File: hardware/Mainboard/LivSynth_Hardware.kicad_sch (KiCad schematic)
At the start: 0 parts

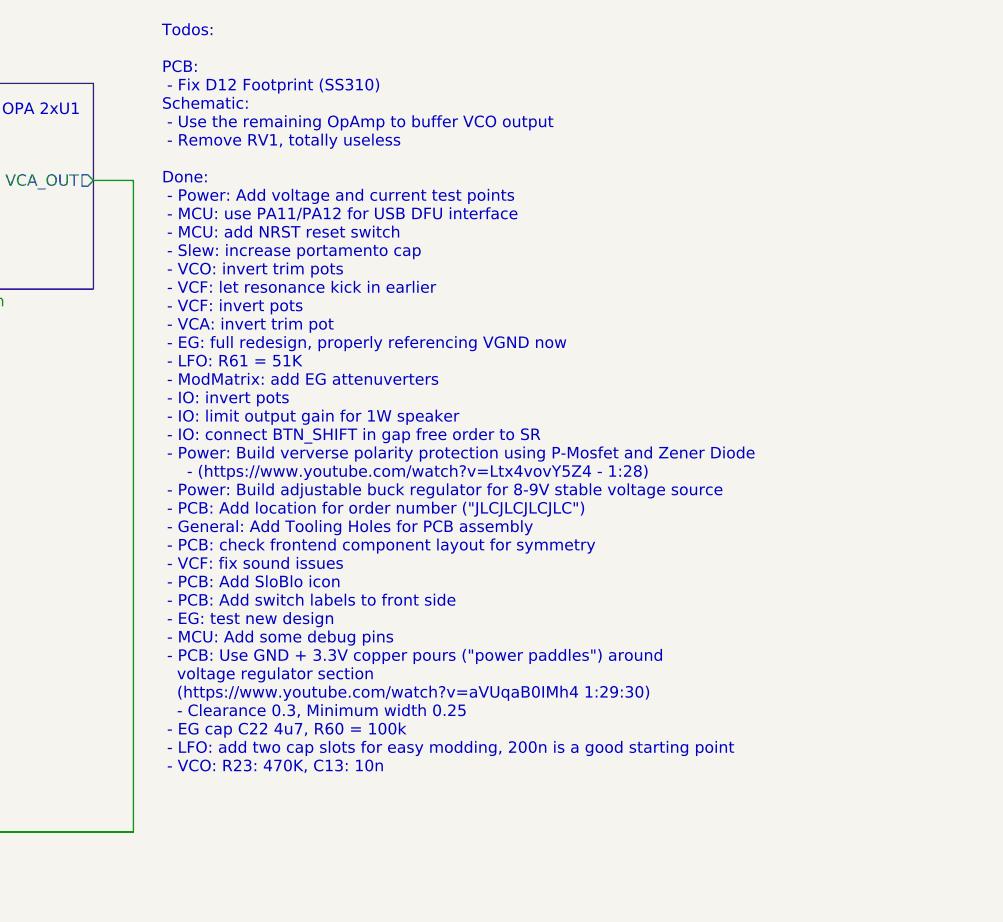
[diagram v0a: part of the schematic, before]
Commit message: add 0v2 status
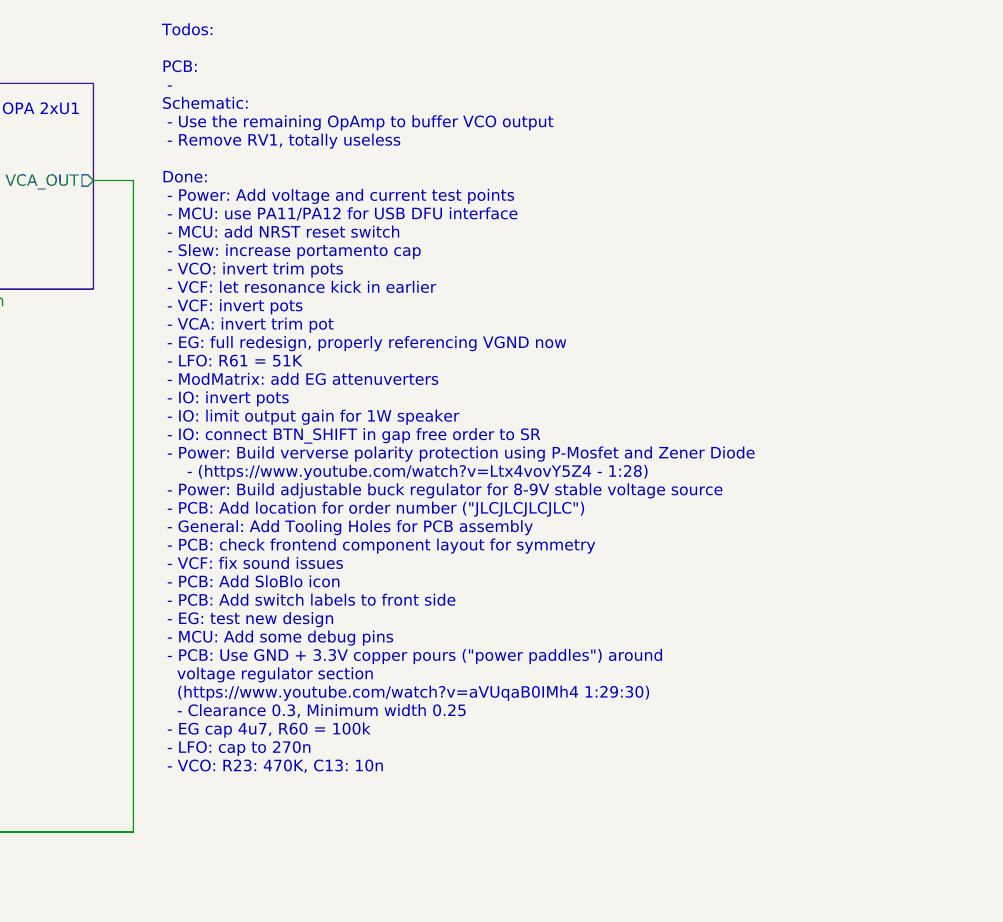
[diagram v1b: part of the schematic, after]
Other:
- note added: "Todos: PCB: - Schematic: - Use the remaining OpAmp to buffer VCO output - Remove RV1, totally useless Done: - Power: Add voltage and current test points - MCU: use PA11/PA12 for USB DFU interface - MCU: add NRST reset switch - Slew: increase portamento cap - VCO: invert trim pots - VCF: let resonance kick in earlier - VCF: invert pots - VCA: invert trim pot - EG: full redesign, properly referenci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"
- note removed: "Todos: PCB: - Fix D12 Footprint (SS310) Schematic: - Use the remaining OpAmp to buffer VCO output - Remove RV1, totally useless Done: - Power: Add voltage and current test points - MCU: use PA11/PA12 for USB DFU interface - MCU: add NRST reset switch - Slew: increase portamento cap - VCO: invert trim pots - VCF: let resonance kick in earlier - VCF: invert pots - VCA: invert trim pot - EG: full re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"
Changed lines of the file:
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@@
     (effects (font (size 1.27 1.27)) (justify left bottom))
   )
-  (text "Todos:\n\nPCB:\n - Fix D12 Footprint (SS310)\nSchematic:\n - Use the remaining OpAmp to buffer VCO output\n - Remove RV1, totally useless\n\nDone:\n - Power: Add voltage and current test points\n - MCU: use PA11/PA12 for USB DFU interface\n - MCU: add NRST reset switch\n - Slew: increase portamento cap\n - VCO: invert trim pots\n - VCF: let resonance kick in earlier\n - VCF: invert pots\n - VCA: invert trim pot\n - EG: full redesign, properly referencing VGND now\n - LFO: R61 = 51K\n - ModMatrix: add EG attenuverters\n - IO: invert pots\n - IO: limit output gain for 1W speaker\n - IO: connect BTN_SHIFT in gap free order to SR\n - Power: Build ververse polarity protection using P-Mosfet and Zener Diode\n     - (https://www.youtube.com/watch?v=Ltx4vovY5Z4 - 1:28)\n - Power: Build adjustable buck regulator for 8-9V stable voltage source\n - PCB: Add location for order number (\"JLCJLCJLCJLC\")\n - General: Add Tooling Holes for PCB assembly\n - PCB: check frontend component layout for symmetry\n - VCF: fix sound issues\n - PCB: Add SloBlo icon\n - PCB: Add switch labels to front side\n - EG: test new design\n - MCU: Add some debug pins\n - PCB: Use GND + 3.3V copper pours (\"power paddles\") around\n   voltage regulator section\n   (https://www.youtube.com/watch?v=aVUqaB0IMh4 1:29:30)\n   - Clearance 0.3, Minimum width 0.25\n - EG cap C22 4u7, R60 = 100k\n - LFO: add two cap slots for easy modding, 200n is a good starting point\n - VCO: R23: 470K, C13: 10n"
+  (text "Todos:\n\nPCB:\n - \nSchematic:\n - Use the remaining OpAmp to buffer VCO output\n - Remove RV1, totally useless\n\nDone:\n - Power: Add voltage and current test points\n - MCU: use PA11/PA12 for USB DFU interface\n - MCU: add NRST reset switch\n - Slew: increase portamento cap\n - VCO: invert trim pots\n - VCF: let resonance kick in earlier\n - VCF: invert pots\n - VCA: invert trim pot\n - EG: full redesign, properly referencing VGND now\n - LFO: R61 = 51K\n - ModMatrix: add EG attenuverters\n - IO: invert pots\n - IO: limit output gain for 1W speaker\n - IO: connect BTN_SHIFT in gap free order to SR\n - Power: Build ververse polarity protection using P-Mosfet and Zener Diode\n     - (https://www.youtube.com/watch?v=Ltx4vovY5Z4 - 1:28)\n - Power: Build adjustable buck regulator for 8-9V stable voltage source\n - PCB: Add location for order number (\"JLCJLCJLCJLC\")\n - General: Add Tooling Holes for PCB assembly\n - PCB: check frontend component layout for symmetry\n - VCF: fix sound issues\n - PCB: Add SloBlo icon\n - PCB: Add switch labels to front side\n - EG: test new design\n - MCU: Add some debug pins\n - PCB: Use GND + 3.3V copper pours (\"power paddles\") around\n   voltage regulator section\n   (https://www.youtube.com/watch?v=aVUqaB0IMh4 1:29:30)\n   - Clearance 0.3, Minimum width 0.25\n - EG cap 4u7, R60 = 100k\n - LFO: cap to 270n\n - VCO: R23: 470K, C13: 10n"
     (at 212.09 99.695 0)
     (effects (font (size 1.27 1.27)) (justify left bottom))

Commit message: Backport from 0v3
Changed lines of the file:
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@@
     (effects (font (size 1.27 1.27)) (justify left bottom))
   )
-  (text "Todos:\n\nPCB:\n - \nSchematic:\n - Use the remaining OpAmp to buffer VCO output\n - Remove RV1, totally useless\n\nDone:\n - Power: Add voltage and current test points\n - MCU: use PA11/PA12 for USB DFU interface\n - MCU: add NRST reset switch\n - Slew: increase portamento cap\n - VCO: invert trim pots\n - VCF: let resonance kick in earlier\n - VCF: invert pots\n - VCA: invert trim pot\n - EG: full redesign, properly referencing VGND now\n - LFO: R61 = 51K\n - ModMatrix: add EG attenuverters\n - IO: invert pots\n - IO: limit output gain for 1W speaker\n - IO: connect BTN_SHIFT in gap free order to SR\n - Power: Build ververse polarity protection using P-Mosfet and Zener Diode\n     - (https://www.youtube.com/watch?v=Ltx4vovY5Z4 - 1:28)\n - Power: Build adjustable buck regulator for 8-9V stable voltage source\n - PCB: Add location for order number (\"JLCJLCJLCJLC\")\n - General: Add Tooling Holes for PCB assembly\n - PCB: check frontend component layout for symmetry\n - VCF: fix sound issues\n - PCB: Add SloBlo icon\n - PCB: Add switch labels to front side\n - EG: test new design\n - MCU: Add some debug pins\n - PCB: Use GND + 3.3V copper pours (\"power paddles\") around\n   voltage regulator section\n   (https://www.youtube.com/watch?v=aVUqaB0IMh4 1:29:30)\n   - Clearance 0.3, Minimum width 0.25\n - EG cap 4u7, R60 = 100k\n - LFO: cap to 270n\n - VCO: R23: 470K, C13: 10n"
+  (text "Todos:\n\nPCB:\n - \nSchematic:\n - Use the remaining OpAmp to buffer VCO output\n - Remove RV1, totally useless\n\nDone:\n - Power: Add voltage and current test points\n - MCU: use PA11/PA12 for USB DFU interface\n - MCU: add NRST reset switch\n - Slew: increase portamento cap\n - VCO: invert trim pots\n - VCF: let resonance kick in earlier\n - VCF: invert pots\n - VCA: invert trim pot\n - EG: full redesign, properly referencing VGND now\n - LFO: R61 = 51K\n - ModMatrix: add EG attenuverters\n - IO: invert pots\n - IO: limit output gain for 1W speaker\n - IO: connect BTN_SHIFT in gap free order to SR\n - Power: Build ververse polarity protection using P-Mosfet and Zener Diode\n     - (https://www.youtube.com/watch?v=Ltx4vovY5Z4 - 1:28)\n - Power: Build adjustable buck regulator for 8-9V stable voltage source\n - PCB: Add location for order number (\"JLCJLCJLCJLC\")\n - General: Add Tooling Holes for PCB assembly\n - PCB: check frontend component layout for symmetry\n - VCF: fix sound issues\n - PCB: Add SloBlo icon\n - PCB: Add switch labels to front side\n - EG: test new design\n - MCU: Add some debug pins\n - PCB: Use GND + 3.3V copper pours (\"power paddles\") around\n   voltage regulator section\n   (https://www.youtube.com/watch?v=aVUqaB0IMh4 1:29:30)\n   - Clearance 0.3, Minimum width 0.25\n - EG cap C22 4u7, R60 = 100K\n - LFO: cap to 270n\n - VCO: R23: 470K, C13: 10n"
     (at 212.09 99.695 0)
     (effects (font (size 1.27 1.27)) (justify left bottom))

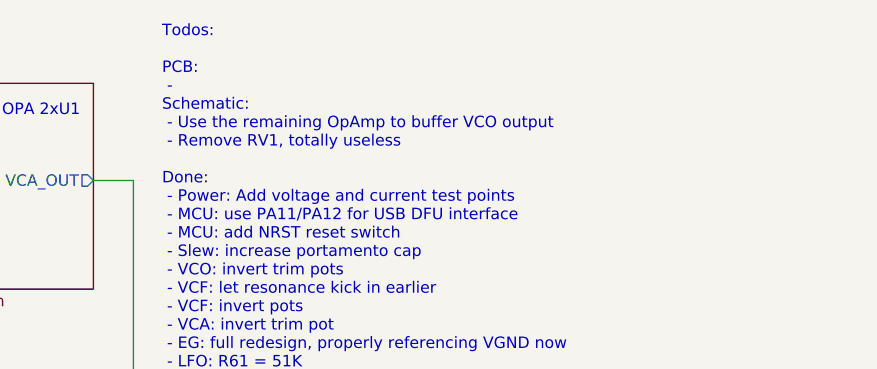
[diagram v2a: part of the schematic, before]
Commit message: Rename Decay -> Release
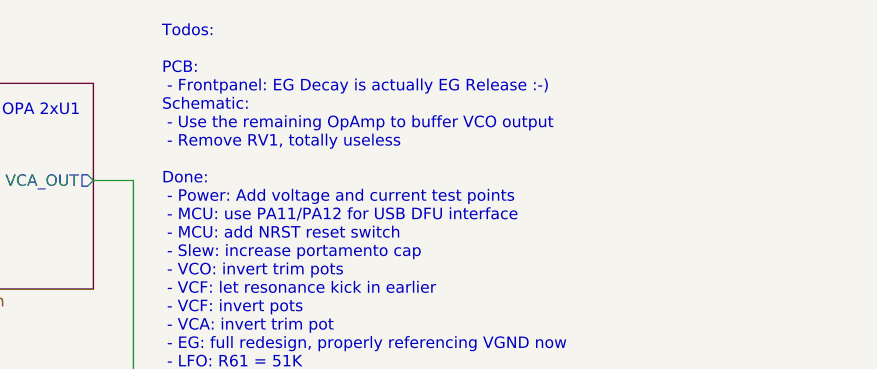
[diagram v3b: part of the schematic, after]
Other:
- note added: "Todos: PCB: - Frontpanel: EG Decay is actually EG Release :-) Schematic: - Use the remaining OpAmp to buffer VCO output - Remove RV1, totally useless Done: - Power: Add voltage and current test points - MCU: use PA11/PA12 for USB DFU interface - MCU: add NRST reset switch - Slew: increase portamento cap - VCO: invert trim pots - VCF: let resonance kick in earlier - VCF: invert pots - VCA: invert 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"
- note removed: "Todos: PCB: - Schematic: - Use the remaining OpAmp to buffer VCO output - Remove RV1, totally useless Done: - Power: Add voltage and current test points - MCU: use PA11/PA12 for USB DFU interface - MCU: add NRST reset switch - Slew: increase portamento cap - VCO: invert trim pots - VCF: let resonance kick in earlier - VCF: invert pots - VCA: invert trim pot - EG: full redesign, properly referenci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"
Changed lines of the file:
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@@
     (effects (font (size 1.27 1.27)) (justify left bottom))
   )
-  (text "Todos:\n\nPCB:\n - \nSchematic:\n - Use the remaining OpAmp to buffer VCO output\n - Remove RV1, totally useless\n\nDone:\n - Power: Add voltage and current test points\n - MCU: use PA11/PA12 for USB DFU interface\n - MCU: add NRST reset switch\n - Slew: increase portamento cap\n - VCO: invert trim pots\n - VCF: let resonance kick in earlier\n - VCF: invert pots\n - VCA: invert trim pot\n - EG: full redesign, properly referencing VGND now\n - LFO: R61 = 51K\n - ModMatrix: add EG attenuverters\n - IO: invert pots\n - IO: limit output gain for 1W speaker\n - IO: connect BTN_SHIFT in gap free order to SR\n - Power: Build ververse polarity protection using P-Mosfet and Zener Diode\n     - (https://www.youtube.com/watch?v=Ltx4vovY5Z4 - 1:28)\n - Power: Build adjustable buck regulator for 8-9V stable voltage source\n - PCB: Add location for order number (\"JLCJLCJLCJLC\")\n - General: Add Tooling Holes for PCB assembly\n - PCB: check frontend component layout for symmetry\n - VCF: fix sound issues\n - PCB: Add SloBlo icon\n - PCB: Add switch labels to front side\n - EG: test new design\n - MCU: Add some debug pins\n - PCB: Use GND + 3.3V copper pours (\"power paddles\") around\n   voltage regulator section\n   (https://www.youtube.com/watch?v=aVUqaB0IMh4 1:29:30)\n   - Clearance 0.3, Minimum width 0.25\n - EG cap C22 4u7, R60 = 100K\n - LFO: cap to 270n\n - VCO: R23: 470K, C13: 10n"
+  (text "Todos:\n\nPCB:\n - Frontpanel: EG Decay is actually EG Release :-)\nSchematic:\n - Use the remaining OpAmp to buffer VCO output\n - Remove RV1, totally useless\n\nDone:\n - Power: Add voltage and current test points\n - MCU: use PA11/PA12 for USB DFU interface\n - MCU: add NRST reset switch\n - Slew: increase portamento cap\n - VCO: invert trim pots\n - VCF: let resonance kick in earlier\n - VCF: invert pots\n - VCA: invert trim pot\n - EG: full redesign, properly referencing VGND now\n - LFO: R61 = 51K\n - ModMatrix: add EG attenuverters\n - IO: invert pots\n - IO: limit output gain for 1W speaker\n - IO: connect BTN_SHIFT in gap free order to SR\n - Power: Build ververse polarity protection using P-Mosfet and Zener Diode\n     - (https://www.youtube.com/watch?v=Ltx4vovY5Z4 - 1:28)\n - Power: Build adjustable buck regulator for 8-9V stable voltage source\n - PCB: Add location for order number (\"JLCJLCJLCJLC\")\n - General: Add Tooling Holes for PCB assembly\n - PCB: check frontend component layout for symmetry\n - VCF: fix sound issues\n - PCB: Add SloBlo icon\n - PCB: Add switch labels to front side\n - EG: test new design\n - MCU: Add some debug pins\n - PCB: Use GND + 3.3V copper pours (\"power paddles\") around\n   voltage regulator section\n   (https://www.youtube.com/watch?v=aVUqaB0IMh4 1:29:30)\n   - Clearance 0.3, Minimum width 0.25\n - EG cap C22 4u7, R60 = 100K\n - LFO: cap to 270n\n - VCO: R23: 470K, C13: 10n"
     (at 212.09 99.695 0)
     (effects (font (size 1.27 1.27)) (justify left bottom))
